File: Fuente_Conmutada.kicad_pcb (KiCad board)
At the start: 2 copper layers, 135 x 85 mm, 47 parts, among them J1 Terminal_220v, J2 Terminal_12v, J3 Vout, Q1 IRF840, Q2 IRF840, T1 Transformer_1P_SS, U1 TL494, U2 IR2110

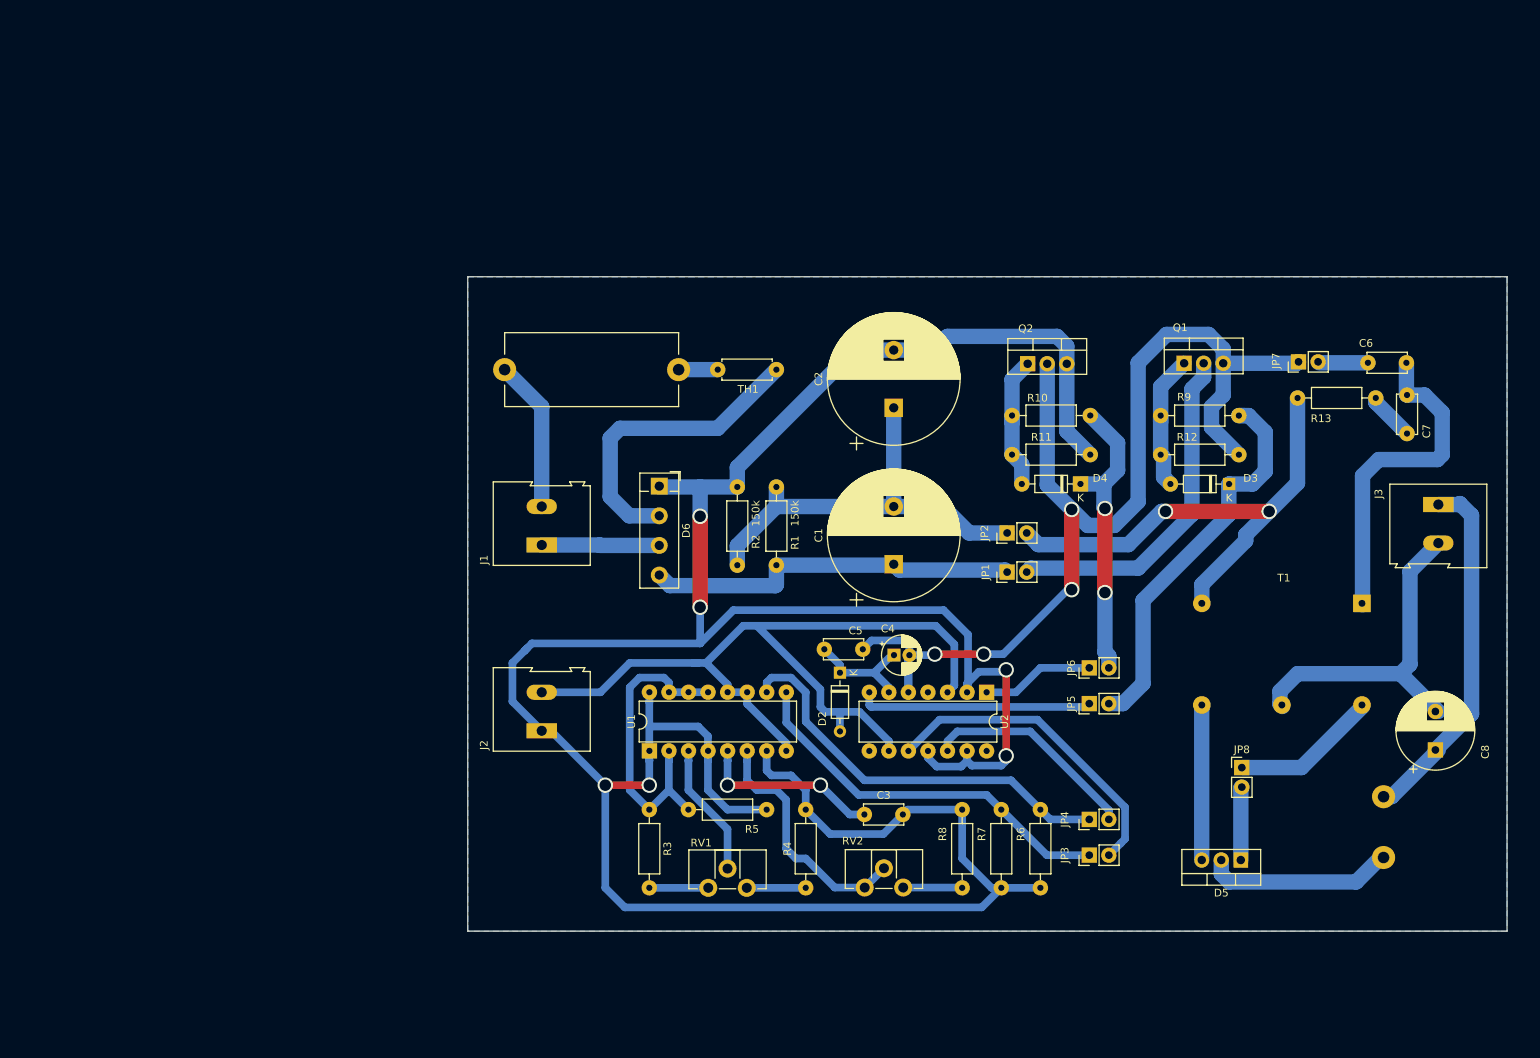
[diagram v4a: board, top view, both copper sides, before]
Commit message: Agregado de cosas
Se agregó:
- Pads de montaje
- Footprints de disipadores para mosfets y rectificador de salida
- Se puso en la capa correcta el choke de salida
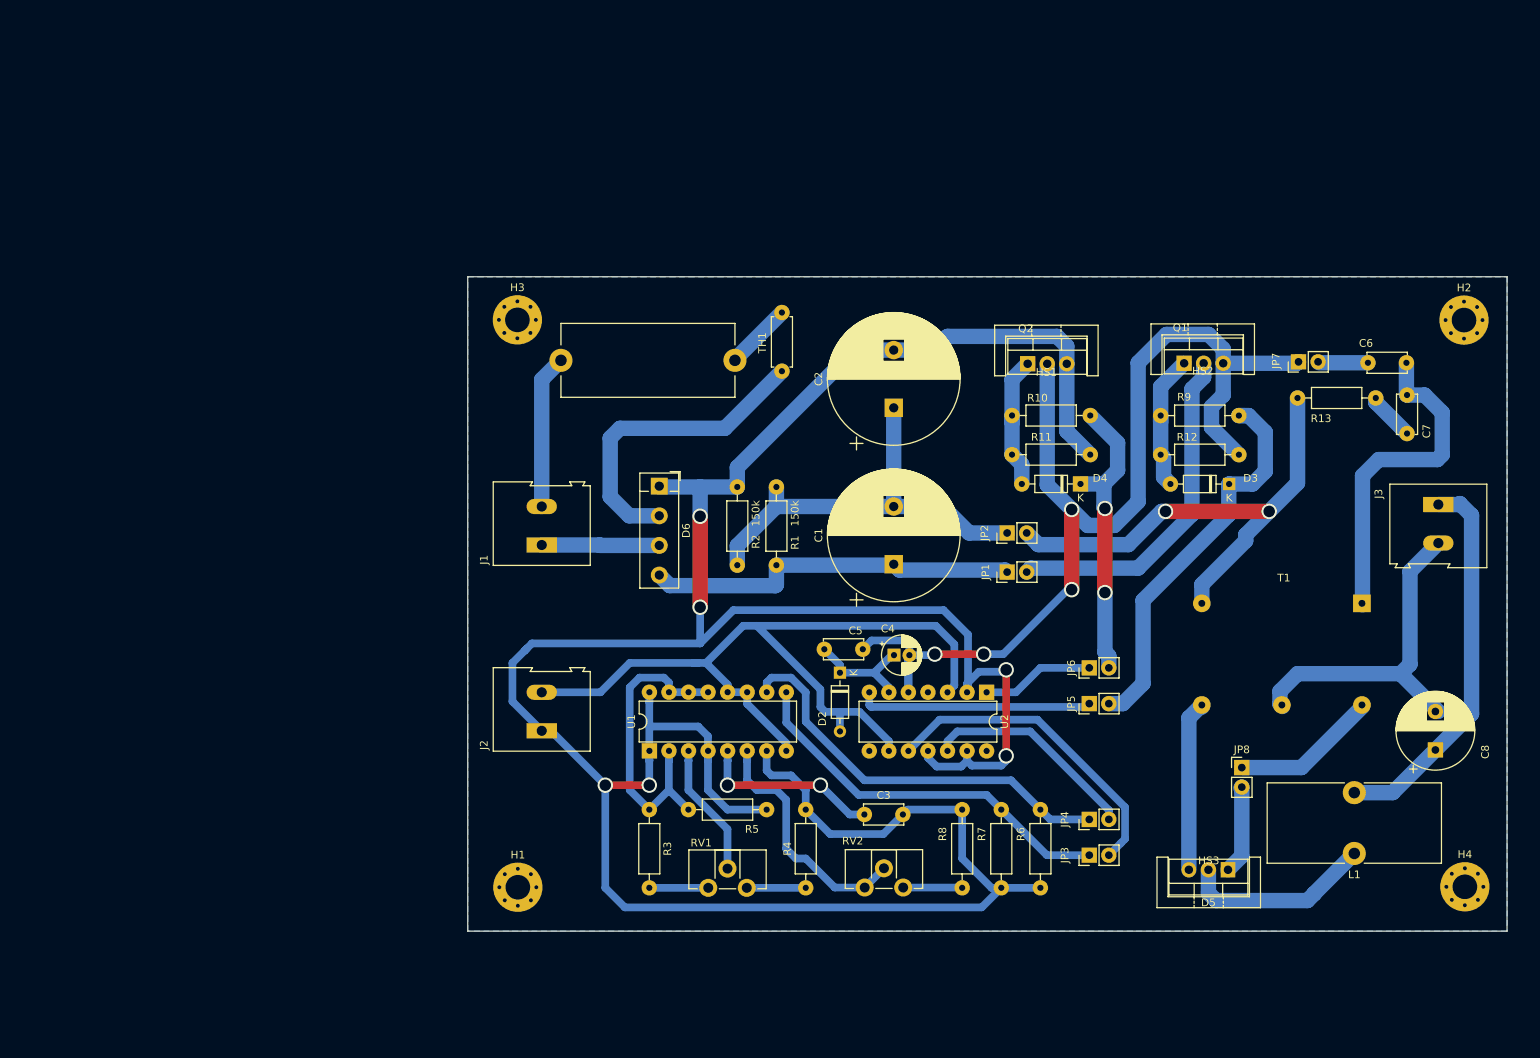
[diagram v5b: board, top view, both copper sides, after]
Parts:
- added H1: MountingHole_Pad, MountingHole:MountingHole_3.2mm_M3_Pad_Via, F.Cu at (82.7, 127.2)
- added H2: MountingHole_Pad, MountingHole:MountingHole_3.2mm_M3_Pad_Via, F.Cu at (205.6, 53.5)
- added H3: MountingHole_Pad, MountingHole:MountingHole_3.2mm_M3_Pad_Via, F.Cu at (82.6, 53.5)
- added H4: MountingHole_Pad, MountingHole:MountingHole_3.2mm_M3_Pad_Via, F.Cu at (205.7, 127.1)
- added HS1: Heatsink, Heatsink:Heatsink_Stonecold_HS-S01_13.21x6.35mm, F.Cu at (151.3, 54.3)
- added HS2: Heatsink, Heatsink:Heatsink_Stonecold_HS-S01_13.21x6.35mm, F.Cu at (171.6, 54.1)
- added HS3: Heatsink, Heatsink:Heatsink_Stonecold_HS-S01_13.21x6.35mm, F.Cu at (172.4, 129.7)
- L1: moved to F.Cu
- moved F1 7.41 mm to (110.9, 58.8)
- moved L1 3.84 mm to (191.3, 122.8), turned to 180 degrees
- moved D5 2.10 mm to (174.9, 124.9)
- moved TH1 0.74 mm to (117.0, 60.2), turned to 90 degrees
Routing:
- net Net-(F1-Pad1): track 5.08 -> 8.74 mm
- net Net-(J3-Pin_1): track 47.1 -> 50.3 mm
- net Net-(D5-A2): track 20.0 -> 22.2 mm
- net Net-(D5-A1): track 9.52 -> 11.7 mm
- net Net-(D6-Pad2): track 40.3 -> 40.9 mm

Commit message: huj
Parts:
- removed D6: B40C2300-1500A, Diode_THT:Diode_Bridge_Vishay_KBPM
- removed H1, H2, H3, H4: MountingHole_Pad, MountingHole:MountingHole_3.2mm_M3_Pad_Via
- removed HS1, HS2, HS3: Heatsink, Heatsink:Heatsink_Stonecold_HS-S01_13.21x6.35mm
- added D1: B80C2300-1500B, Diode_THT:Diode_Bridge_Vishay_KBPM, F.Cu at (101.0, 75.2)
- L1: moved to B.Cu
- moved F1 7.41 mm to (103.5, 60.0)
- moved L1 3.84 mm to (195.1, 123.3), turned to 0 degrees
- moved D5 2.10 mm to (176.6, 123.7)
- moved TH1 0.74 mm to (116.2, 60.0), turned to 180 degrees
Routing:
- net Net-(F1-Pad1): track 8.74 -> 5.08 mm
- net Net-(J3-Pin_1): track 50.3 -> 47.1 mm
- net Net-(D1-+): track 48.8 -> 51.9 mm
- net Net-(D5-A2): track 22.2 -> 20.0 mm
- net Net-(D5-A1): track 11.7 -> 9.52 mm
- net GND_AC: track 15.3 -> 16.9 mm
- net +12V: track 111.1 -> 112.6 mm
- net Net-(D1-Pad2): track 40.9 -> 40.3 mm
- net (no net): vias 0 -> 4
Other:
- board size 135 x 85 mm -> 140 x 95 mm

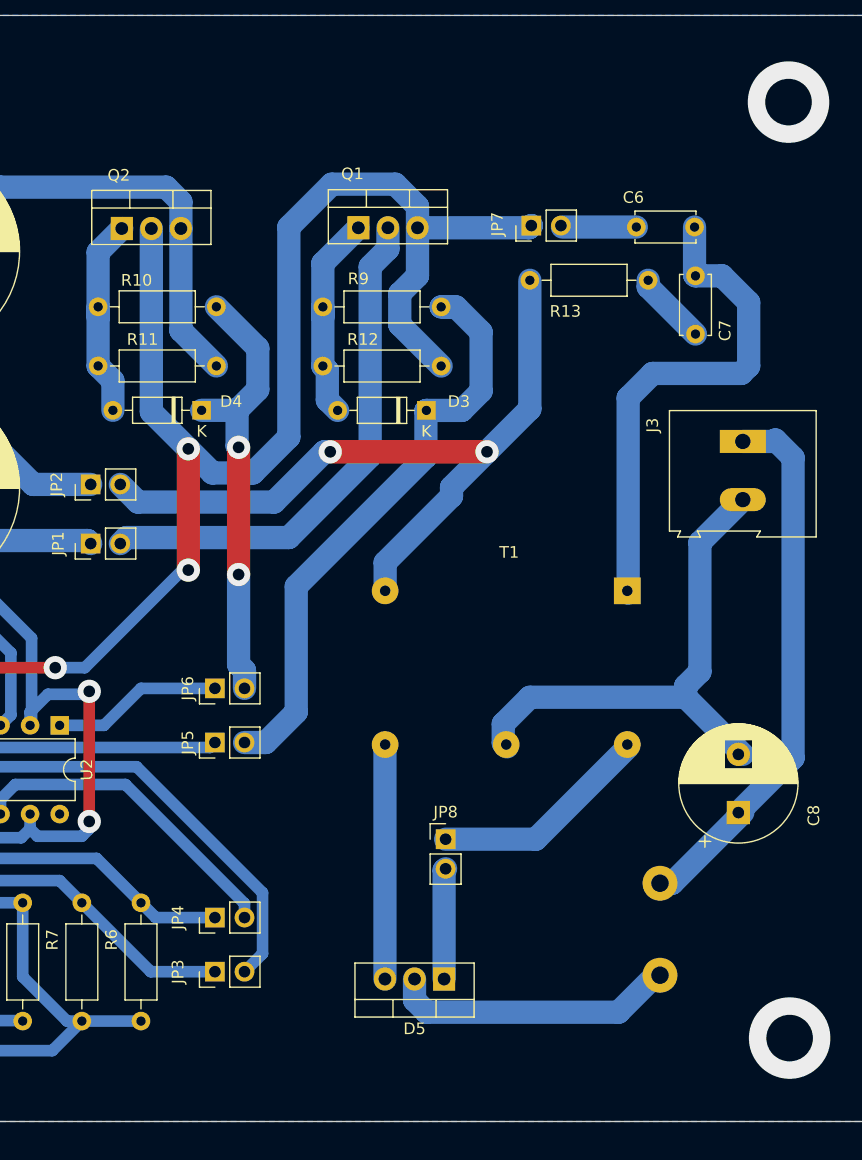
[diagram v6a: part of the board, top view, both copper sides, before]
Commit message: Agregado de disipadores
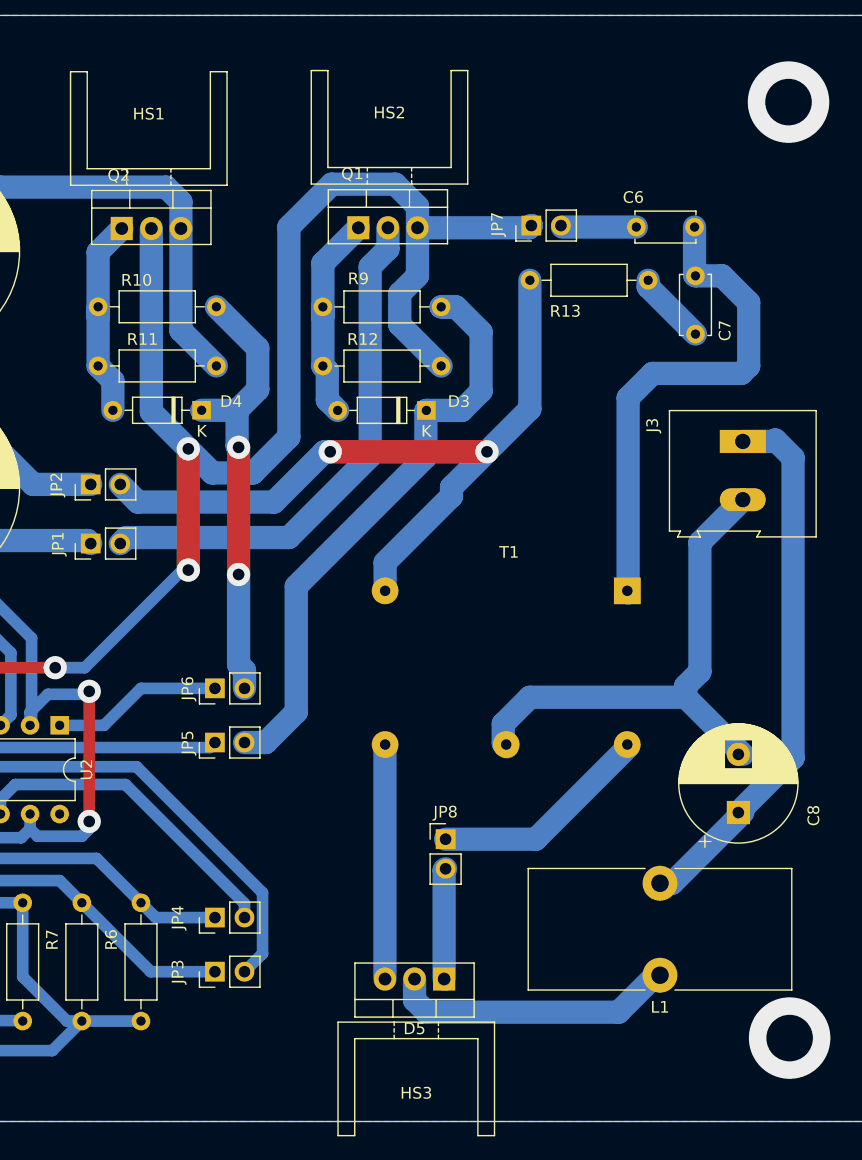
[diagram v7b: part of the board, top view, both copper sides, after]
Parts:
- added HS1: Heatsink, Heatsink:Heatsink_Stonecold_HS-S02_13.21x9.53mm, F.Cu at (151.2, 55.4)
- added HS2: Heatsink, Heatsink:Heatsink_Stonecold_HS-S02_13.21x9.53mm, F.Cu at (171.9, 55.3)
- added HS3: Heatsink, Heatsink:Heatsink_Stonecold_HS-S02_13.21x9.53mm, F.Cu at (174.2, 127.5)
- L1: moved to F.Cu
- turned L1 to 180 degrees

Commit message: test
-Le hice test en el esquematico y pcb
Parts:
- moved D5 0.24 mm to (176.4, 123.4)
- moved Q2 0.21 mm to (148.8, 59.4)
